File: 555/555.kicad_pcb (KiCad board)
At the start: 2 copper layers, 10 parts, among them U1 LM555xM, U2 TSOP17xx

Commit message: 555 para imprimir
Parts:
- moved R3 41.0 mm to (129.5, 51.1), turned to -90 degrees
- moved R4 32.7 mm to (119.7, 70.6), turned to 180 degrees
- moved R2 28.8 mm to (132.0, 51.0)
- moved U1 28.3 mm to (131.2, 61.0)
- moved C1 24.7 mm to (125.8, 57.9), turned to 90 degrees
- moved U2 21.6 mm to (122.0, 50.5)
- moved D1 20.9 mm to (118.1, 56.6)
- moved RV1 20.6 mm to (116.4, 66.6), turned to -90 degrees
- moved R1 20.1 mm to (120.4, 66.4), turned to 90 degrees
- moved C2 15.8 mm to (122.0, 52.9), turned to -90 degrees
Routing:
- net +5V: track 0.00 -> 30.6 mm
- net Net-(U1-THR): track 0.00 -> 26.9 mm
- net GND: track 0.00 -> 20.1 mm
- net Net-(U1-DIS): track 0.00 -> 16.1 mm
- net Net-(D1-A): track 0.00 -> 14.3 mm
- net Net-(U2-GND): track 0.00 -> 13.8 mm
- net Net-(D1-K): track 0.00 -> 11.3 mm
- net Net-(U1-R): track 0.00 -> 3.31 mm
- net Sensores: track 0.00 -> 2.51 mm
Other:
- board text added: "Gerli"

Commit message: 555 para imprimir
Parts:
- moved U1 0.47 mm to (131.1, 61.4)
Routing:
- net Net-(U2-GND): track 13.8 -> 16.2 mm
- net +5V: track 30.6 -> 31.1 mm

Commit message: ana
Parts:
- removed R3: 22k, Resistor_THT:R_Axial_DIN0204_L3.6mm_D1.6mm_P5.08mm_Horizontal
- added J1: Conn_01x03_Pin, Connector_PinHeader_2.54mm:PinHeader_1x03_P2.54mm_Vertical, F.Cu at (140.3, 56.1)
- moved U2 22.6 mm to (143.8, 56.1)
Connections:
- R1 pad 2: Net-(U1-R) -> +5V
- U1 pad 4: Net-(U1-R) -> +5V
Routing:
- net Net-(U1-R): track 3.09 -> 0.00 mm
- net Sensores: track 2.51 -> 0.00 mm
- net +5V: track 31.1 -> 31.7 mm

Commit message: lalalalal
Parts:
- added ?: , , F.Cu at (210.5, 28.3)
- added C3: 104, Capacitor_THT:C_Disc_D4.3mm_W1.9mm_P5.00mm, F.Cu at (195.7, 42.8)
- added C4: 104, Capacitor_THT:C_Disc_D4.3mm_W1.9mm_P5.00mm, F.Cu at (51.1, 48.0)
- added D2: LED, LED_THT:LED_D5.0mm_Horizontal_O1.27mm_Z3.0mm, F.Cu at (44.1, 41.4)
- added D3: LED, LED_THT:LED_D5.0mm_Horizontal_O1.27mm_Z3.0mm, F.Cu at (206.4, 39.2)
- added Q1: BC547, Package_TO_SOT_THT:TO-92_Wide, F.Cu at (118.1, 48.0)
- added R3: 4.7k, Resistor_SMD:R_1206_3216Metric_Pad1.30x1.75mm_HandSolder, B.Cu at (115.5, 54.0)
- added R5: 100, Resistor_SMD:R_1206_3216Metric_Pad1.30x1.75mm_HandSolder, B.Cu at (195.1, 48.5)
- added R6: 100, Resistor_THT:R_Axial_DIN0207_L6.3mm_D2.5mm_P10.16mm_Horizontal, F.Cu at (47.5, 49.0)
- added R7: 100, Resistor_THT:R_Axial_DIN0207_L6.3mm_D2.5mm_P10.16mm_Horizontal, F.Cu at (199.4, 50.6)
- added R8: 100, Resistor_SMD:R_1206_3216Metric_Pad1.30x1.75mm_HandSolder, B.Cu at (49.3, 42.1)
- added REF**: MountingHole_3.2mm_M3_Pad, MountingHole:MountingHole_3.2mm_M3_Pad, F.Cu at (39.2, 28.4)
- added U3: TSOP17xx, Package_TO_SOT_THT:TO-92S_Wide, F.Cu at (192.1, 42.8)
- added U4: TSOP17xx, Package_TO_SOT_THT:TO-92S_Wide, F.Cu at (52.6, 39.1)
- J1: value Conn_01x03_Pin -> Conn_02x05_Counter_Clockwise; footprint Connector_PinHeader_2.54mm:PinHeader_1x03_P2.54mm_Vertical -> Connector_IDC:IDC-Header_2x05_P2.54mm_Horizontal
- R1, R2: footprint Resistor_THT:R_Axial_DIN0204_L3.6mm_D1.6mm_P5.08mm_Horizontal -> Resistor_SMD:R_1206_3216Metric_Pad1.30x1.75mm_HandSolder; moved to B.Cu
- R4: footprint Resistor_THT:R_Axial_DIN0204_L3.6mm_D1.6mm_P5.08mm_Horizontal -> Resistor_THT:R_Axial_DIN0207_L6.3mm_D2.5mm_P10.16mm_Horizontal; moved to B.Cu
- moved J1 30.1 mm to (167.8, 43.9), turned to -90 degrees
- moved U2 26.9 mm to (121.7, 40.9)
- moved R4 21.0 mm to (129.4, 51.9), turned to 90 degrees
- moved D1 12.7 mm to (117.2, 43.9)
- moved R1 9.78 mm to (130.2, 66.6), turned to 0 degrees
- moved R2 5.76 mm to (133.4, 56.6)
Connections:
- D1 pad 1: Net-(D1-K) -> 38khz
- J1 pad 1: +5V -> Sensores_2
- J1 pad 2: GND -> +5V
- J1 pad 3: Sensores -> unconnected-(J1-Pin_3-Pad3)
- U1 pad 3: Net-(D1-K) -> Net-(U1-Q)
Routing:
- net 38khz: track 0.00 -> 191.3 mm
- net +5V: track 31.7 -> 152.4 mm, vias 0 -> 2
- net Sensores_3: track 0.00 -> 120.1 mm, vias 0 -> 2
- net GND: track 20.4 -> 132.6 mm, vias 0 -> 3
- net Sensores_2: track 0.00 -> 49.2 mm
- net Sensores: track 0.00 -> 33.8 mm
- net Net-(U2-GND): track 16.2 -> 32.6 mm, vias 0 -> 2
- net Net-(U1-Q): track 0.00 -> 16.0 mm
- net Net-(D1-K): track 11.7 -> 0.00 mm
- net Net-(U3-GND): track 0.00 -> 11.3 mm
- net Net-(U4-GND): track 0.00 -> 11.0 mm
- net Net-(D1-A): track 14.5 -> 24.5 mm
- net Net-(D3-A): track 0.00 -> 3.23 mm
- net Net-(D2-A): track 0.00 -> 3.11 mm
- net Net-(U1-DIS): track 16.3 -> 18.8 mm
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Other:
- board outline added: 182.1 x 71.3 mm
- board text removed: "Gerli"

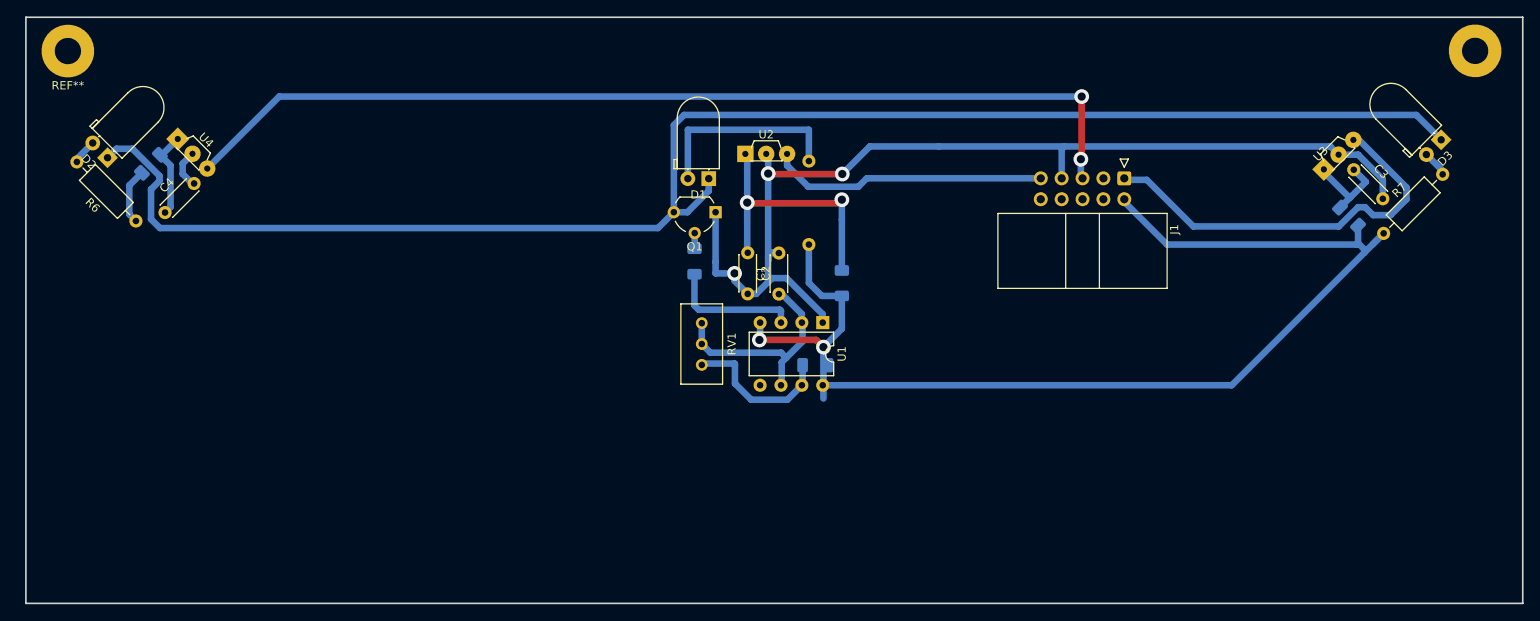
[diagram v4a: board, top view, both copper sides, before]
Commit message: pcb 555 centrada
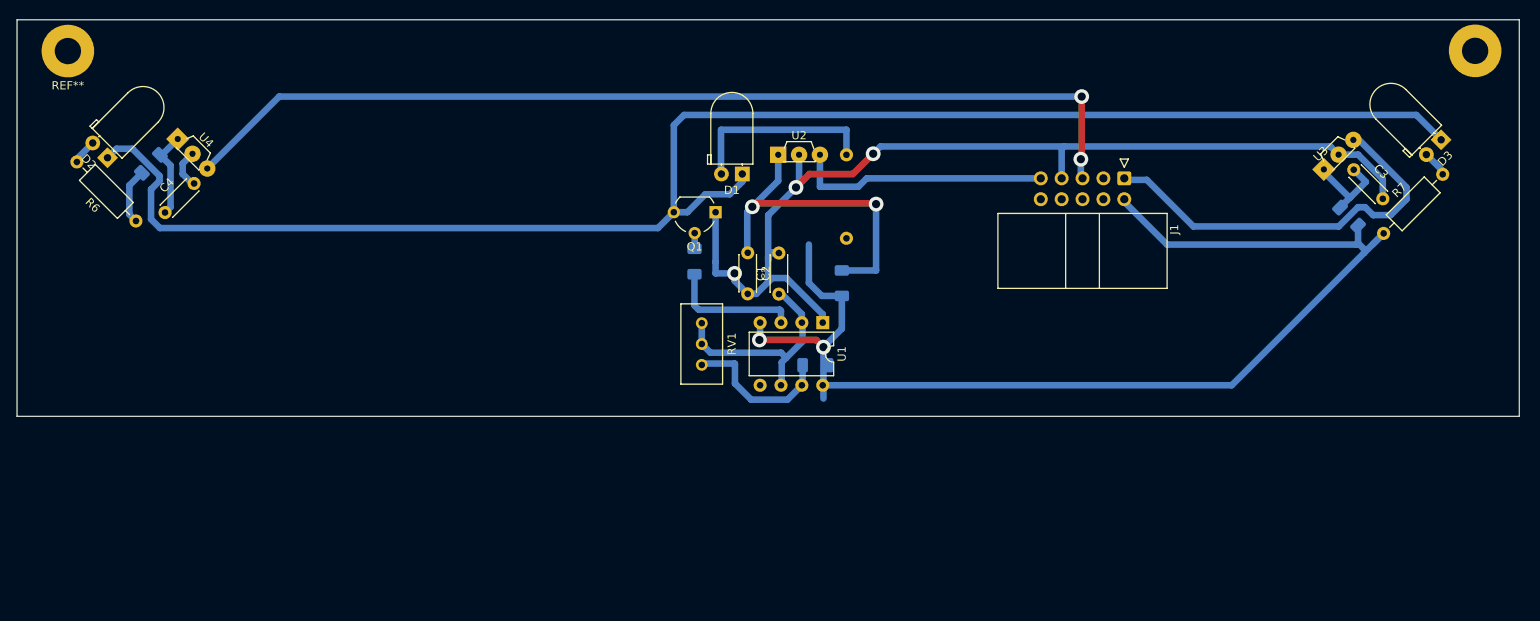
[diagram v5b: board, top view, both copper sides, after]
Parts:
- moved R4 4.64 mm to (134.0, 51.2)
- moved D1 4.12 mm to (121.3, 43.3)
- moved U2 4.00 mm to (125.7, 41.0)
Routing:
- net Net-(U2-GND): track 32.6 -> 41.0 mm
- net 38khz: track 191.3 -> 195.2 mm
- net Sensores: track 33.8 -> 31.2 mm
- net GND: track 132.6 -> 131.2 mm
- net Net-(D1-A): track 24.5 -> 23.7 mm
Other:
- board size 182.1 x 71.3 mm -> 182.8 x 48.3 mm

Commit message: falta revisar
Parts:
- moved R3 0.61 mm to (115.5, 54.6)
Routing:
- net GND: track 131.2 -> 320.1 mm
- net +5V: track 152.4 -> 235.1 mm
- net Net-(U1-Q): track 16.0 -> 13.6 mm

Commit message: para imprimir
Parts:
- moved R2 11.1 mm to (124.5, 50.0), turned to 0 degrees
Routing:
- net Net-(U2-GND): track 41.0 -> 15.5 mm, vias 2 -> 1
- net GND: track 320.1 -> 324.4 mm
- net +5V: track 235.1 -> 230.9 mm
- net Sensores: track 31.2 -> 34.5 mm

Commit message: soporte tof
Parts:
- R4: footprint Resistor_THT:R_Axial_DIN0207_L6.3mm_D2.5mm_P10.16mm_Horizontal -> Resistor_SMD:R_1206_3216Metric_Pad1.30x1.75mm_HandSolder
- moved RV1 42.1 mm to (83.5, 40.2), turned to 90 degrees
- moved R1 38.4 mm to (99.9, 43.1)
- moved U1 38.1 mm to (99.7, 39.7)
- moved C1 36.1 mm to (97.0, 36.1), turned to 0 degrees
- moved R3 29.3 mm to (88.8, 42.6), turned to -90 degrees
- moved C2 16.8 mm to (105.2, 51.7), turned to 90 degrees
- moved Q1 10.4 mm to (107.8, 46.2), turned to 0 degrees
- moved R4 3.61 mm to (133.9, 47.5)
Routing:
- net GND: track 324.4 -> 383.8 mm, vias 3 -> 2
- net +5V: track 230.9 -> 265.8 mm, vias 2 -> 4
- net Net-(Q1-B): track 1.91 -> 36.2 mm
- net Net-(U1-THR): track 27.1 -> 51.0 mm
- net Net-(U2-GND): track 15.5 -> 28.6 mm, vias 1 -> 0
- net Net-(U1-DIS): track 18.8 -> 30.8 mm
- net Net-(U1-Q): track 13.6 -> 7.68 mm
- net Net-(D1-A): track 23.7 -> 28.8 mm
- net 38khz: track 195.8 -> 198.9 mm
- net Sensores_3: track 120.1 -> 122.1 mm
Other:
- board size 182.8 x 48.3 mm -> 182.8 x 33.6 mm
